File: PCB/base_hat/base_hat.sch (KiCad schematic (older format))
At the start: 15 parts, among them M1 Fan_4pin, P1 Conn_02x20_Odd_Even, U1 DS3231MZ

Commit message: add fab file for JLCPCB
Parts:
- C1: LCSC (none) -> C179466; LCSC Part C179466 -> (none)
- R1, R2: LCSC (none) -> C17414; LCSC Part C165963 -> (none)
- U1: LCSC (none) -> C107410; LCSC Part C107410 -> (none)

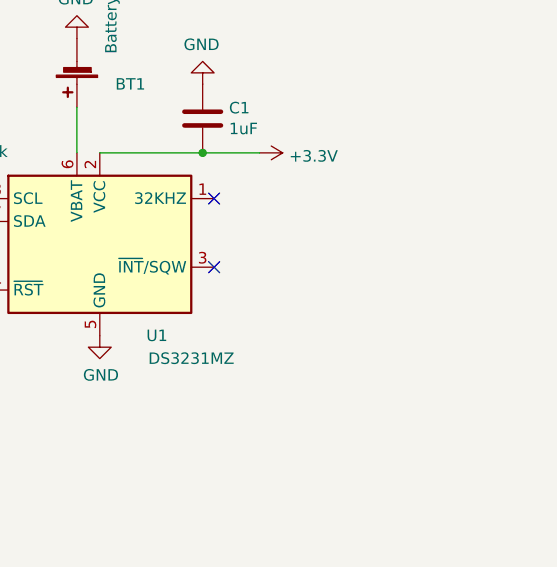
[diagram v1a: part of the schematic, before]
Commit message: add hexa i2c adress
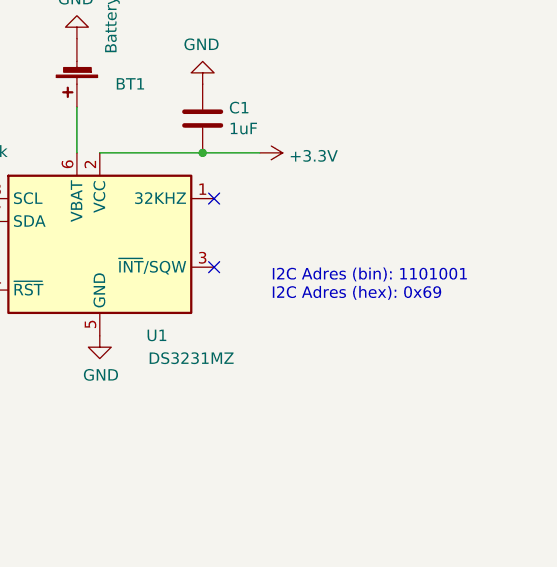
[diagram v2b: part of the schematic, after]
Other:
- note added: "I2C Adres (bin): 1101001\nI2C Adres (hex): 0x69"
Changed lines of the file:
@@
 	1    0    0    -1
 $EndComp
+Text Notes 7050 2900 0    50   ~ 0
+I2C Adres (bin): 1101001\nI2C Adres (hex): 0x69
 $EndSCHEMATC
